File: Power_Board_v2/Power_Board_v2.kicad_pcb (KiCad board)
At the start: 2 copper layers, 33 parts, among them J1 Conn_02x16_Odd_Even, Q1 MMBT5551L, U2 HUSB237-AA001-DN06R, U3 BQ24074RGT, U4 INA219AxDCN SOT-23

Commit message: Did some PCB work
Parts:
- removed C1, C2: 1u, Capacitor_SMD:C_0201_0603Metric_Pad0.64x0.40mm_HandSolder
- removed C3: 4.7u, Capacitor_SMD:C_0201_0603Metric_Pad0.64x0.40mm_HandSolder
- removed R1: 0.4R, Resistor_SMD:R_0805_2012Metric_Pad1.20x1.40mm_HandSolder
- removed R5: 10k, Resistor_SMD:R_0201_0603Metric_Pad0.64x0.40mm_HandSolder
- removed R6, R8: 1k5, Resistor_SMD:R_0201_0603Metric_Pad0.64x0.40mm_HandSolder
- added C6: 1u, Capacitor_SMD:C_0201_0603Metric_Pad0.64x0.40mm_HandSolder, F.Cu at (154.1, 45.8)
- added C7: 1u, Capacitor_SMD:C_0201_0603Metric_Pad0.64x0.40mm_HandSolder, F.Cu at (144.3, 106.9)
- added C8: 4.7u, Capacitor_SMD:C_0201_0603Metric_Pad0.64x0.40mm_HandSolder, F.Cu at (164.1, 51.8)
- added R15: 1k5, Resistor_SMD:R_0201_0603Metric_Pad0.64x0.40mm_HandSolder, F.Cu at (142.2, 60.8)
- added R16: 10k, Resistor_SMD:R_0201_0603Metric_Pad0.64x0.40mm_HandSolder, F.Cu at (144.3, 102.9)
- added R17: 0.4R, Resistor_SMD:R_0805_2012Metric_Pad1.20x1.40mm_HandSolder, F.Cu at (137.9, 112.9)
- added R18: 1k5, Resistor_SMD:R_0201_0603Metric_Pad0.64x0.40mm_HandSolder, F.Cu at (167.1, 55.8)
- D1: value LED -> LEDW
- D2: value LED -> LEDR
- moved C4 71.1 mm to (161.1, 48.8)
- moved Q1 67.2 mm to (147.7, 65.8)
- moved R4 45.5 mm to (148.7, 76.8)
- moved R9 45.2 mm to (148.1, 47.8)
- moved R7 36.8 mm to (154.7, 62.8)
- moved R11 36.2 mm to (150.7, 52.8)
- moved R13 35.8 mm to (155.2, 54.8)
- moved R12 35.3 mm to (155.7, 50.8)
- moved D2 33.7 mm to (146.1, 54.8)
- moved D1 32.0 mm to (146.1, 53.1)
- moved TP4 23.9 mm to (63.2, 85.3)
- moved TP5 23.9 mm to (68.2, 80.2)
- moved TP6 23.9 mm to (68.2, 85.3)
- moved R2 23.2 mm to (104.6, 129.0), turned to -90 degrees
- moved C5 22.3 mm to (120.0, 130.0), turned to -90 degrees
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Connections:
- R11 pad 1: GND -> Net-(Q1-E)
- R11 pad 2: Net-(U3-ILIM) -> GND
- R12 pad 1: /FAST_CHARGE_CTRL -> GND
- R12 pad 2: Net-(Q1-B) -> Net-(U3-ILIM)
- R14 pad 1: Net-(U4-IN+) -> /BATT
- TP1 pad 1: Net-(U4-IN+) -> /BATT
- U4 pad 1: Net-(U4-IN+) -> /BATT
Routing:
- net GND: track 55.8 -> 7.03 mm
- net /I2C1_SDA: track 0.62 -> 18.8 mm
- net /I2C1_SCL: track 0.00 -> 15.5 mm
- net /BATT: track 6.39 -> 16.3 mm
- net /5V Out: track 0.00 -> 9.46 mm
- net Net-(U4-A1): track 0.07 -> 8.78 mm
- net Net-(U2-VSET): track 3.99 -> 10.7 mm
- net Net-(U4-IN+): track 6.49 -> 0.00 mm
- net Net-(U4-A0): track 0.00 -> 6.24 mm
- net Net-(U2-CC1): track 11.5 -> 6.20 mm
- net Net-(U2-CC2): track 11.7 -> 11.9 mm, vias 0 -> 2

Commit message: More PCB work
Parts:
- moved C8 65.3 mm to (141.1, 113.0)
- moved R9 64.9 mm to (152.7, 112.6), turned to -90 degrees
- moved C6 62.6 mm to (161.3, 108.0)
- moved D1 62.5 mm to (152.3, 115.2)
- moved D2 62.5 mm to (152.3, 117.0)
- moved C4 62.2 mm to (159.3, 111.0)
- moved R18 59.1 mm to (156.7, 114.0), turned to -90 degrees
- moved R12 54.4 mm to (150.7, 105.0), turned to 180 degrees
- moved R11 50.5 mm to (162.3, 102.0)
- moved R13 46.3 mm to (151.1, 101.0), turned to 180 degrees
- moved R7 45.5 mm to (141.7, 106.4), turned to 90 degrees
- moved Q1 37.8 mm to (158.8, 102.0)
- moved R15 37.8 mm to (145.7, 98.4), turned to 90 degrees
- moved R3 34.6 mm to (154.7, 103.4), turned to -90 degrees
- moved R4 31.7 mm to (154.7, 108.0), turned to -90 degrees
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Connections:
- C4 pad 1: GND -> /LOAD
- Q1 pad 3: GND -> Net-(Q1-C)
- R13 pad 1: GND -> Net-(Q1-C)
- R3 pad 1: GND -> Net-(Q1-C)
- TP3 pad 1: GND -> Net-(Q1-C)
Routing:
- net /BATT: track 16.3 -> 41.9 mm
- net /High Voltage (9V): track 19.4 -> 38.4 mm
- net /I2C1_SDA: track 18.8 -> 1.63 mm
- net /LOAD: track 0.00 -> 16.6 mm
- net /I2C1_SCL: track 15.5 -> 0.07 mm
- net Net-(Q1-B): track 0.00 -> 13.0 mm
- net Net-(U3-ISET): track 0.00 -> 11.7 mm
- net Net-(Q1-C): track 0.00 -> 11.5 mm
- net Net-(D2-K): track 0.00 -> 7.61 mm
- net Net-(U3-ILIM): track 0.00 -> 6.07 mm
- net Net-(D1-K): track 0.00 -> 5.71 mm
- net Net-(U3-TS): track 0.00 -> 5.11 mm
- net Net-(D2-A): track 0.00 -> 5.11 mm
- net Net-(Q1-E): track 0.00 -> 4.43 mm
- net Net-(R3-Pad2): track 0.00 -> 3.16 mm
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
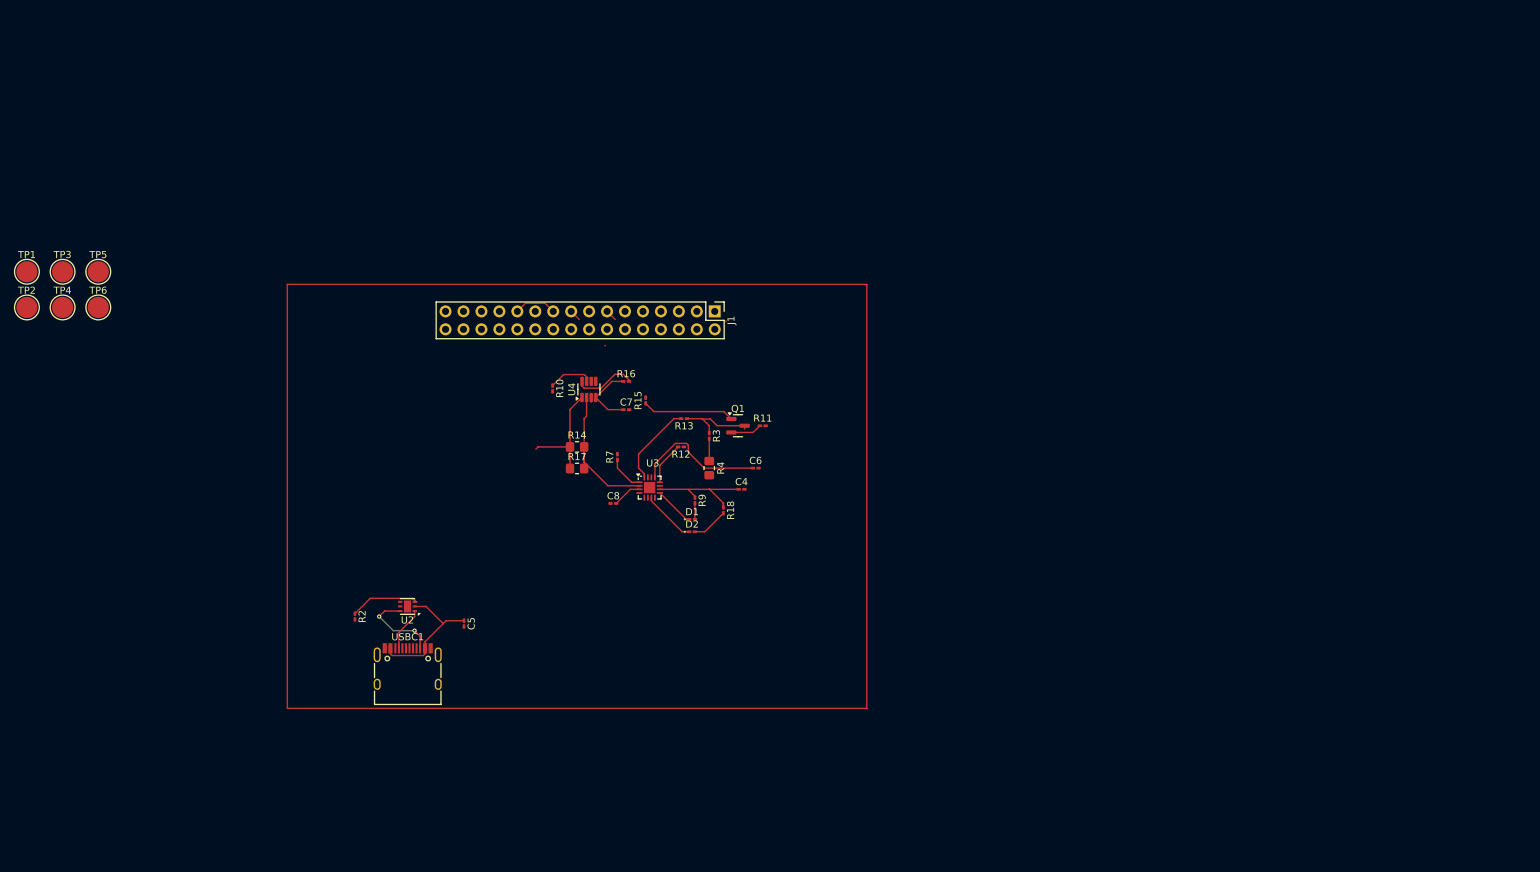
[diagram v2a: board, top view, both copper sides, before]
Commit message: Space Saving
Moved my things around to make space for Ebi's work
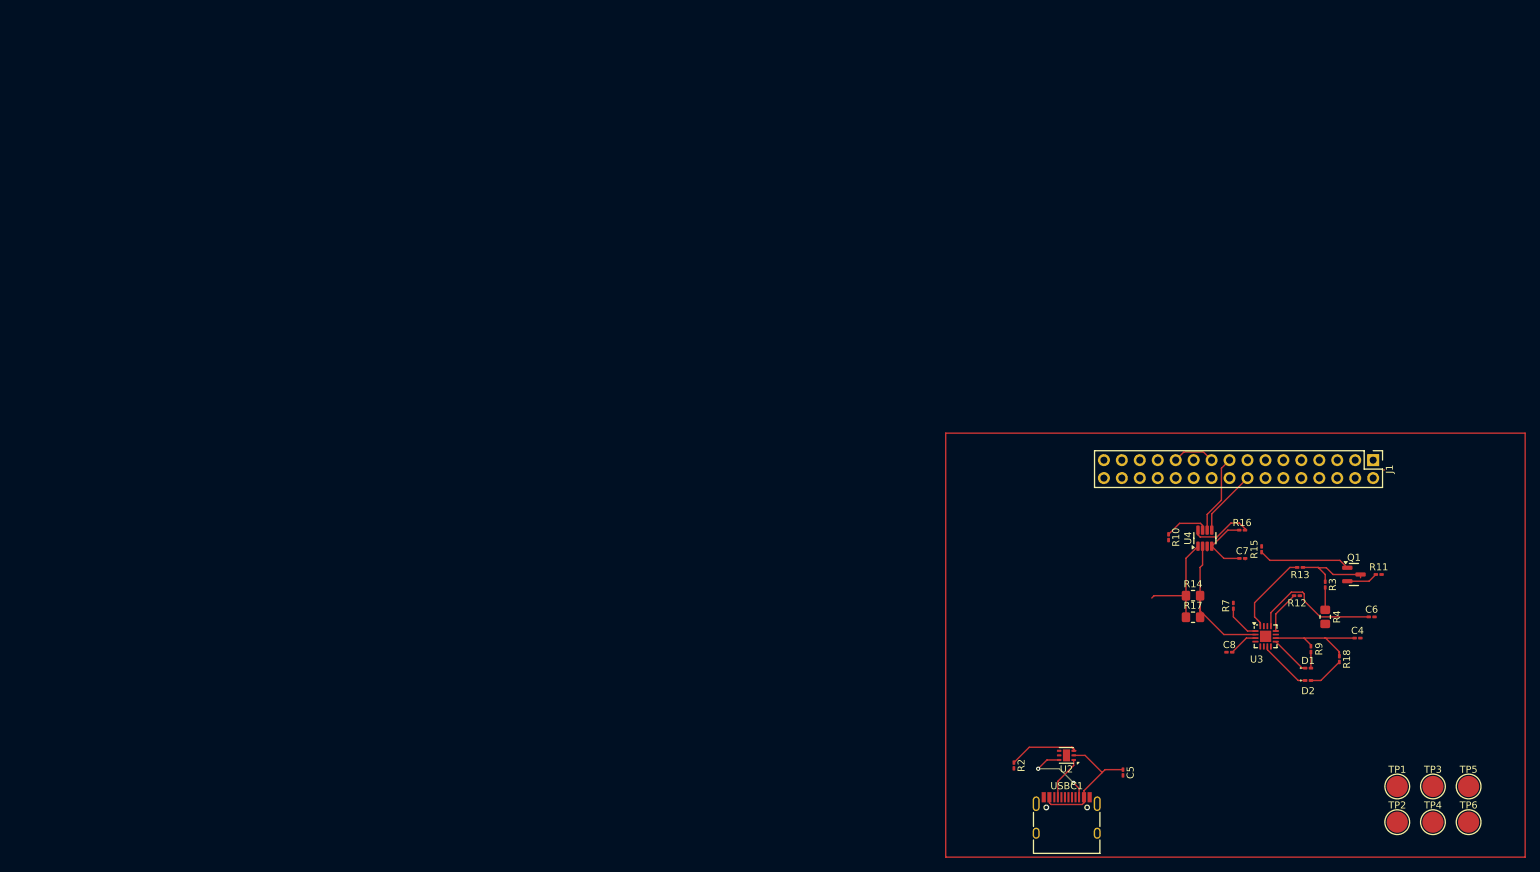
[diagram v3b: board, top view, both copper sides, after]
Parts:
- moved TP1 207.1 mm to (252.1, 153.1)
- moved TP2 207.1 mm to (252.1, 158.1)
- moved TP3 207.1 mm to (257.1, 153.1)
- moved TP4 207.1 mm to (257.1, 158.1)
- moved TP5 207.1 mm to (262.2, 153.1)
- moved TP6 207.1 mm to (262.2, 158.1)
- moved USBC1 95.6 mm to (205.3, 158.6)
- moved C5 95.6 mm to (213.3, 151.1)
- moved R2 95.6 mm to (197.8, 150.1)
- moved U2 95.6 mm to (205.3, 148.6)
- moved J1 95.5 mm to (248.7, 106.9)
- moved C4 89.7 mm to (246.4, 132.1)
- moved C6 89.7 mm to (248.4, 129.1)
- moved C7 89.7 mm to (230.1, 120.8)
- moved C8 89.7 mm to (228.3, 134.1)
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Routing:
- net /I2C1_SDA: track 1.63 -> 11.2 mm
- net /I2C1_SCL: track 0.07 -> 9.46 mm
- net /FAST_CHARGE_CTRL: track 1.74 -> 0.11 mm
